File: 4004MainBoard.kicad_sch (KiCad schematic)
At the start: 103 parts

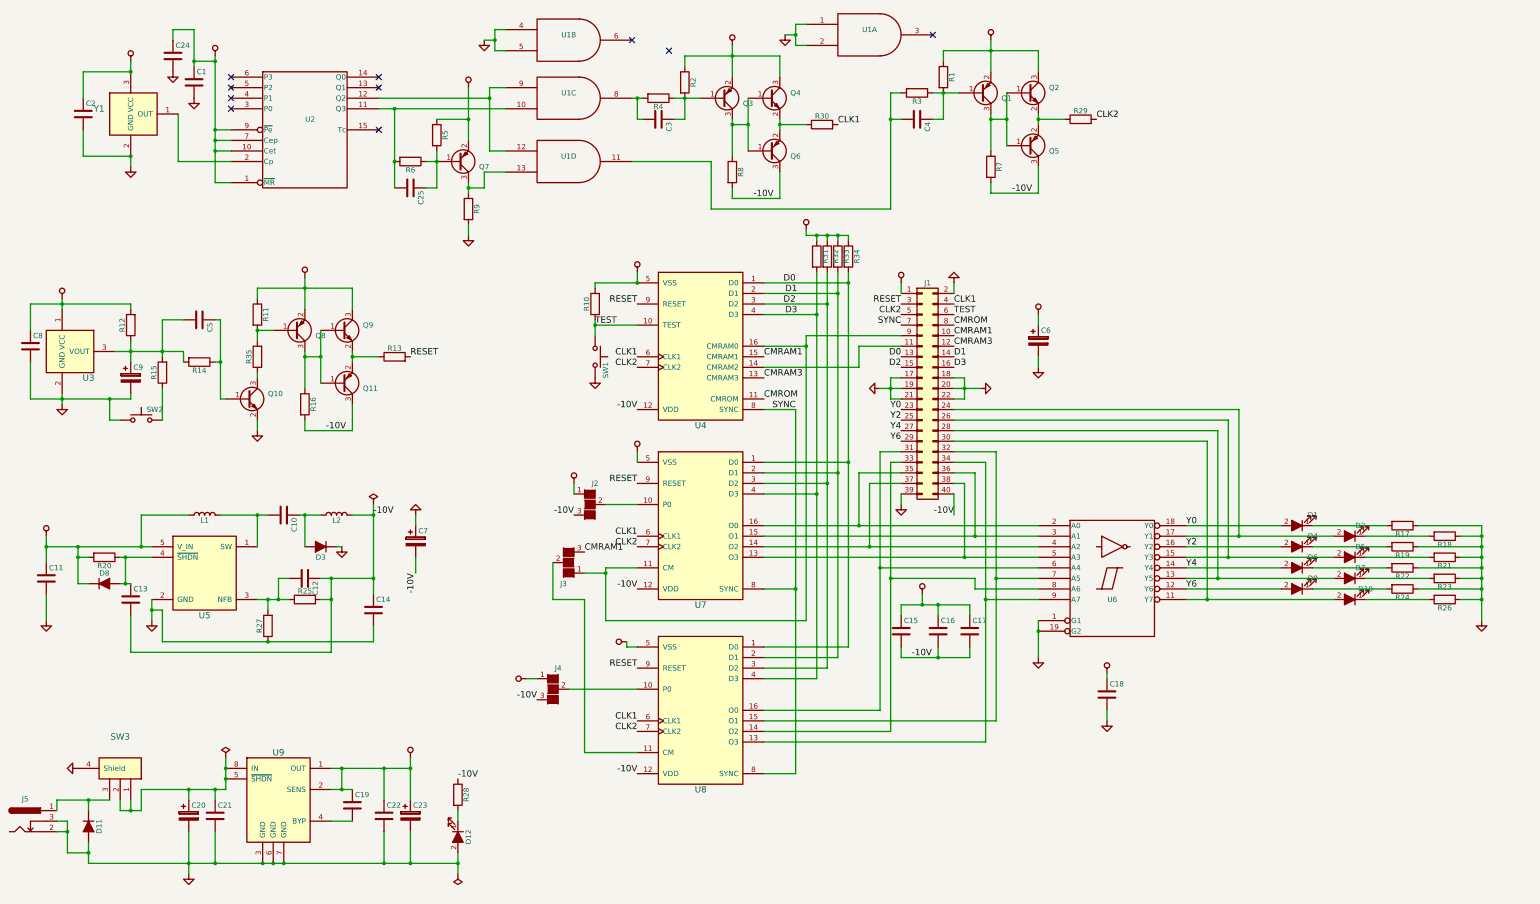
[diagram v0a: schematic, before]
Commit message: migrate to KiCad 7
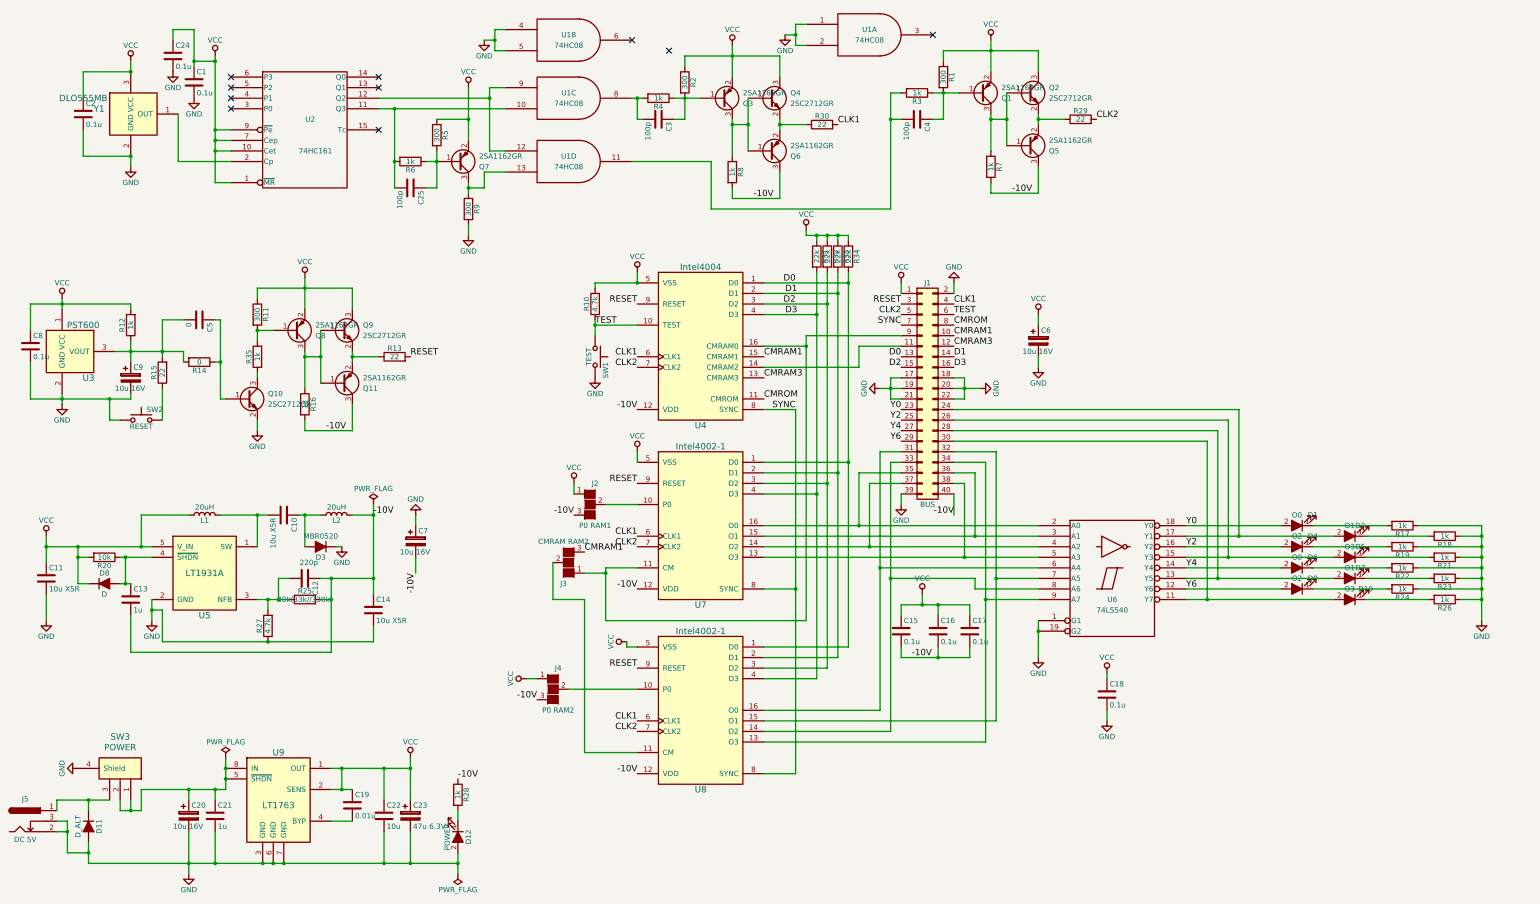
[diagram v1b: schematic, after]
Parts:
- C1, C15, C16, C17, C18, C2, C24, C8: value (none) -> 0.1u; footprint (none) -> Capacitors_SMD:C_0603_HandSoldering
- C10, C11, C14: value (none) -> 10u X5R; footprint (none) -> Capacitors_SMD:C_1206_HandSoldering
- C12: value (none) -> 220p; footprint (none) -> Capacitors_SMD:C_0603_HandSoldering
- C13, C21: value (none) -> 1u; footprint (none) -> Capacitors_SMD:C_0603_HandSoldering
- C19: value (none) -> 0.01u; footprint (none) -> Capacitors_SMD:C_0603_HandSoldering
- C20, C6, C7, C9: value (none) -> 10u 16V; footprint (none) -> Capacitors_SMD:CP_Elec_4x4.5
- C22: value (none) -> 10u; footprint (none) -> Capacitors_SMD:C_1206_HandSoldering
- C23: value (none) -> 47u 6.3V; footprint (none) -> Capacitors_SMD:CP_Elec_5x5.8
- C25, C3, C4: value (none) -> 100p; footprint (none) -> Capacitors_SMD:C_0603_HandSoldering
- C5: value (none) -> 0; footprint (none) -> Capacitors_SMD:C_0603_HandSoldering
- D1, D6: value (none) -> O0; footprint (none) -> LEDs:LED_0603_HandSoldering
- D10, D5: value (none) -> O3; footprint (none) -> LEDs:LED_0603_HandSoldering
- D11: value (none) -> D_ALT; footprint (none) -> cd_device:D_SOD-123_HandSoldering
- D12: value (none) -> POWER; footprint (none) -> LEDs:LED_0603_HandSoldering
- D2, D7: value (none) -> O1; footprint (none) -> LEDs:LED_0603_HandSoldering
- D3: value (none) -> MBR0520; footprint (none) -> cd_device:D_SOD-123_HandSoldering
- D4, D9: value (none) -> O2; footprint (none) -> LEDs:LED_0603_HandSoldering
- D8: value (none) -> D; footprint (none) -> cd_device:D_SOD-123_HandSoldering
- J1: value (none) -> BUS; footprint (none) -> Pin_Headers:Pin_Header_Straight_2x20_Pitch2.54mm
- J2: value (none) -> P0 RAM1; footprint (none) -> Connect:GS3
- J3: value (none) -> CMRAM RAM2; footprint (none) -> Connect:GS3
- J4: value (none) -> P0 RAM2; footprint (none) -> Connect:GS3
- J5: value (none) -> DC 5V; footprint (none) -> cd_device:DC_JACK_MJ-179PH
- L1, L2: value (none) -> 20uH; footprint (none) -> Choke_SMD:Choke_SMD_10.4x10.4_H4.8
- Q1, Q11, Q3, Q5, Q6, Q7, Q8: value (none) -> 2SA1162GR; footprint (none) -> TO_SOT_Packages_SMD:SC-59_Handsoldering
- Q10, Q2, Q4, Q9: value (none) -> 2SC2712GR; footprint (none) -> TO_SOT_Packages_SMD:SC-59_Handsoldering
- R1, R11, R2, R5, R9: value (none) -> 300; footprint (none) -> Resistors_SMD:R_0603_HandSoldering
- R10, R27: value (none) -> 4.7k; footprint (none) -> Resistors_SMD:R_0603_HandSoldering
- R12, R16, R17, R18, R19, R21, R22, R23, R24, R26, R28, R3, R35, R4, R6, R7, R8: value (none) -> 1k; footprint (none) -> Resistors_SMD:R_0603_HandSoldering
- R13, R15, R29, R30: value (none) -> 22; footprint (none) -> Resistors_SMD:R_0603_HandSoldering
- R14: value (none) -> 0; footprint (none) -> Resistors_SMD:R_0603_HandSoldering
- R20: value (none) -> 10k; footprint (none) -> Resistors_SMD:R_0603_HandSoldering
- R25: value (none) -> 30k(33k//330k); footprint (none) -> Resistors_SMD:R_0603_HandSoldering
- R31, R32, R33, R34: value (none) -> 22k; footprint (none) -> Resistors_SMD:R_0603_HandSoldering
- SW1: value (none) -> TEST; footprint (none) -> Buttons_Switches_ThroughHole:SW_PUSH_6mm
- SW2: value (none) -> RESET; footprint (none) -> Buttons_Switches_ThroughHole:SW_PUSH_6mm
- SW3: value (none) -> POWER; footprint (none) -> cd_device:ToggleSW_MS-612A_RI
- U1: value (none) -> 74HC08; footprint (none) -> cd_device:SOIC-14_3.9_5.3x8.7mm_P1.27mm
- U2: value (none) -> 74HC161; footprint (none) -> cd_device:SOIC-16_3.9_5.3x10.2mm_P1.27mm
- U3: value (none) -> PST600; footprint (none) -> TO_SOT_Packages_THT:TO-92_Inline_Wide
- U4: value (none) -> Intel4004; footprint (none) -> Housings_DIP:DIP-16_W7.62mm_Socket
- U5: value (none) -> LT1931A; footprint (none) -> TO_SOT_Packages_SMD:TSOT-23-5_HandSoldering
- U6: value (none) -> 74LS540; footprint (none) -> Housings_SOIC:SOIC-20W_7.5x12.8mm_Pitch1.27mm
- U7, U8: value (none) -> Intel4002-1; footprint (none) -> Housings_DIP:DIP-16_W7.62mm_Socket
- U9: value (none) -> LT1763; footprint (none) -> Housings_SOIC:SOIC-8_3.9x4.9mm_Pitch1.27mm
- Y1: value (none) -> DLO555MB; footprint (none) -> TO_SOT_Packages_THT:TO-92_Inline_Wide

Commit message: update descrete buffer add notes
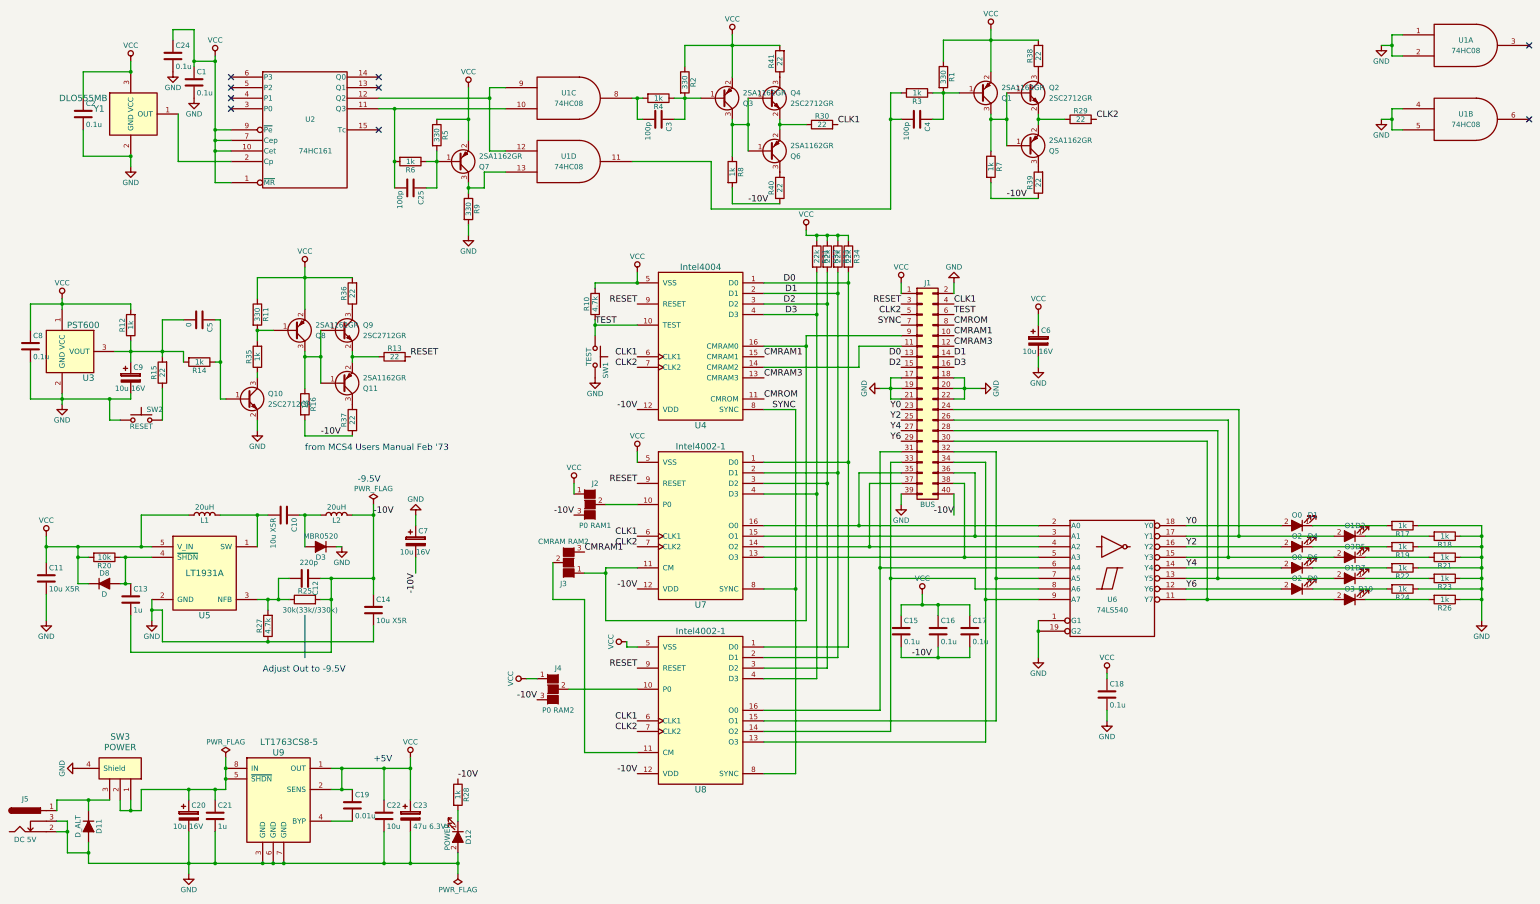
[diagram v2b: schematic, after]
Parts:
- added R36, R37, R38, R39, R40, R41: 22, Resistor_SMD:R_0603_1608Metric_Pad0.98x0.95mm_HandSolder, symbol 4004MainBoard-rescue:R
- C1, C12, C13, C15, C16, C17, C18, C19, C2, C21, C24, C25, C3, C4, C5, C8: footprint Capacitors_SMD:C_0603_HandSoldering -> Capacitor_SMD:C_0603_1608Metric_Pad1.08x0.95mm_HandSolder
- R1, R11, R2, R5, R9: value 300 -> 330; footprint Resistors_SMD:R_0603_HandSoldering -> Resistor_SMD:R_0603_1608Metric_Pad0.98x0.95mm_HandSolder
- R10, R12, R13, R15, R16, R17, R18, R19, R20, R21, R22, R23, R24, R25, R26, R27, R28, R29, R3, R30, R31, R32, R33, R34, R35, R4, R6, R7, R8: footprint Resistors_SMD:R_0603_HandSoldering -> Resistor_SMD:R_0603_1608Metric_Pad0.98x0.95mm_HandSolder
- R14: value 0 -> 1k; footprint Resistors_SMD:R_0603_HandSoldering -> Resistor_SMD:R_0603_1608Metric_Pad0.98x0.95mm_HandSolder
- U9: value LT1763 -> LT1763CS8-5
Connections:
- net -10V: now also R37.1, R39.1, R40.1; no longer Q11.3 (C), Q5.3 (C), Q6.3 (C)
- net VCC: now also R36.2, R38.2, R41.2; no longer Q2.3 (C), Q4.3 (C), Q9.3 (C)
- new net: Q4.3 (C), R41.1
- new net: Q6.3 (C), R40.2
- new net: Q2.3 (C), R38.1
- new net: Q5.3 (C), R39.2
- new net: Q9.3 (C), R36.1
- new net: Q11.3 (C), R37.2
- no-connect marks 10 -> 9
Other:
- note added: "+5V"
- note added: "-9.5V"
- note added: "Adjust Out to -9.5V"
- note added: "from MCS4 Users Manual Feb '73"
- moved on the sheet: U1A, U1B
